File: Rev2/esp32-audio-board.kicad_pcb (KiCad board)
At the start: 4 copper layers, 37.5 x 70 mm, 129 parts, among them IC1 LP2985A-33DBVR, J2 JST S2B, J21 IO32_PAD0, J3 USB_C_Receptacle_USB2.0_16P, J5 IO32_PAD1, J6 IO33_PAD0, J7 IO33_PAD1, J8 IO25_PAD0, J9 IO25_PAD1, Q1 SS8050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

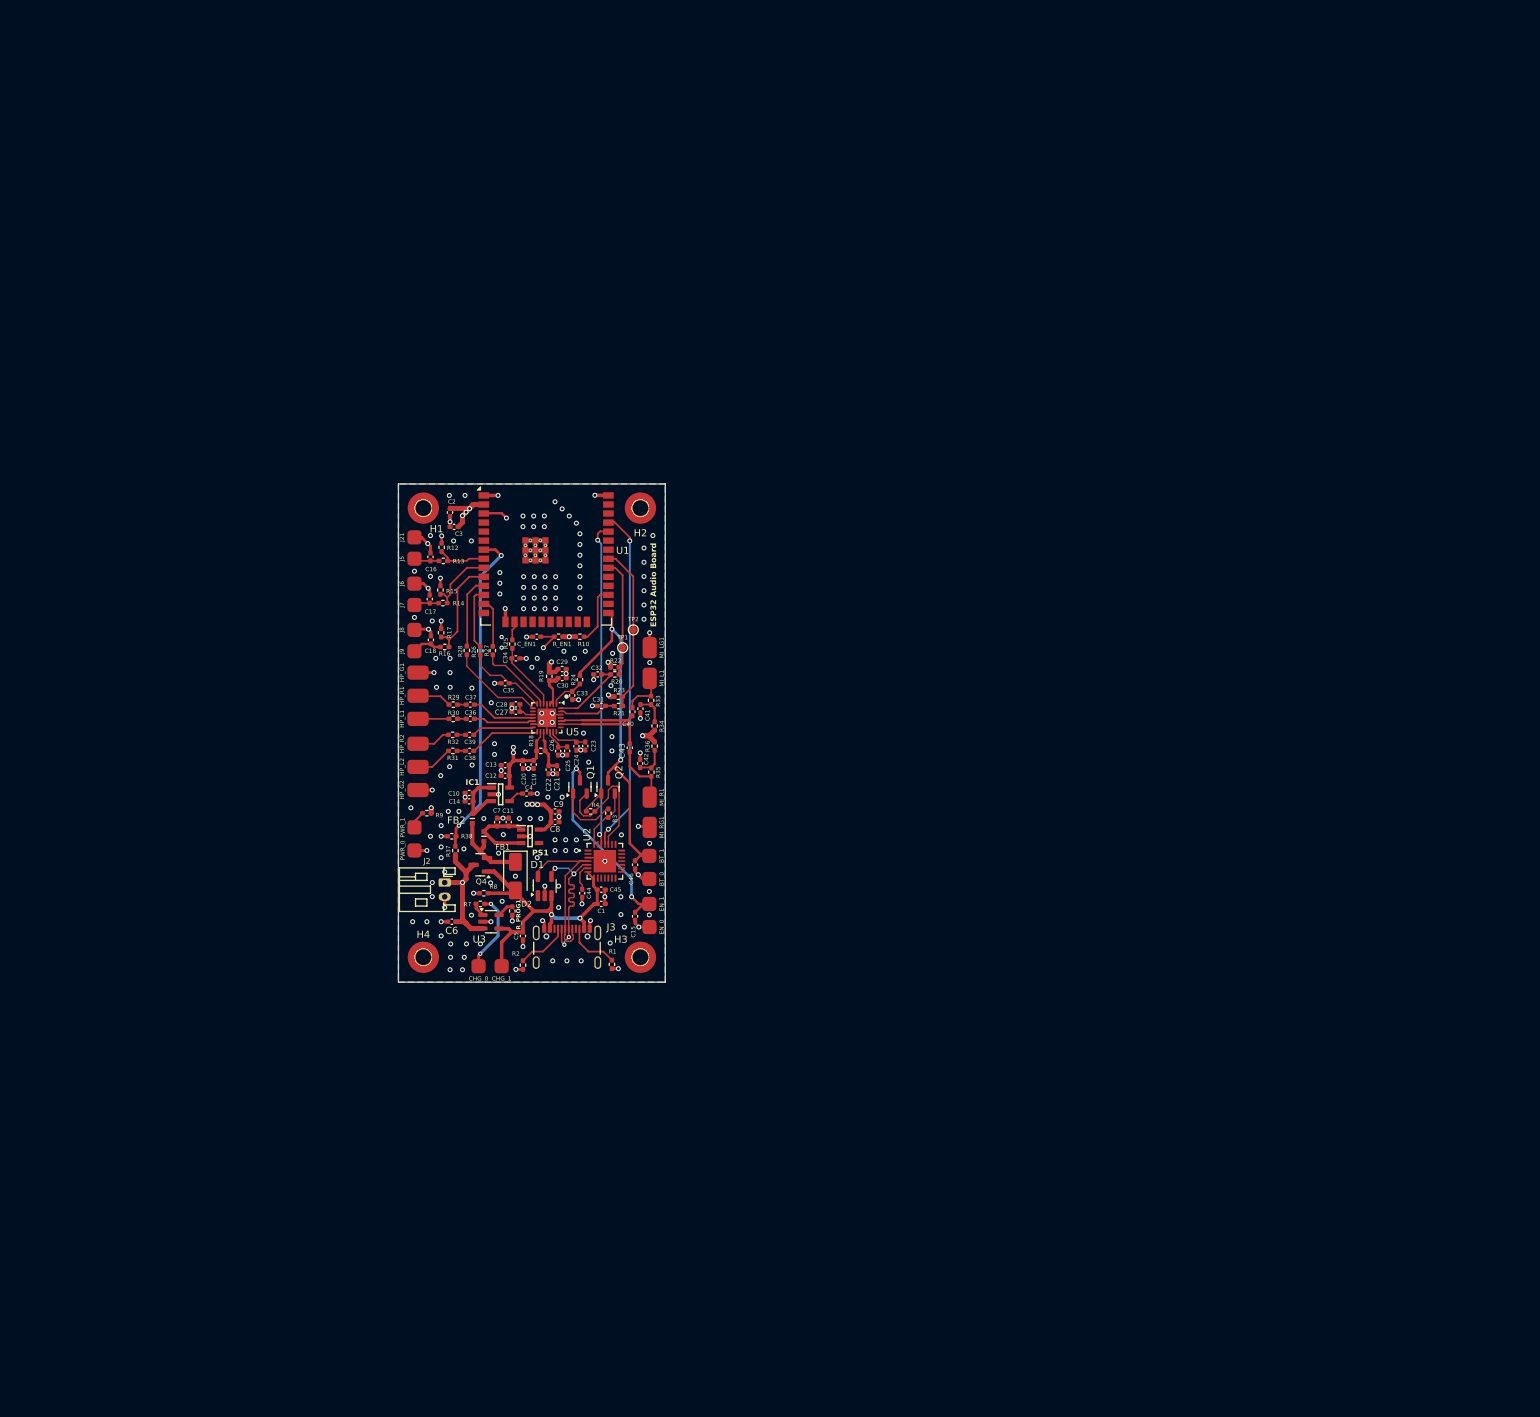
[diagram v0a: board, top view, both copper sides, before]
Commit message: esp32-audio-board: initial Rev2 PCB
Started working on the Rev2 PCB. Managed to get components
a lot closer and the PCB layout is more compact. The PCB
width got smaller by ~10mm.
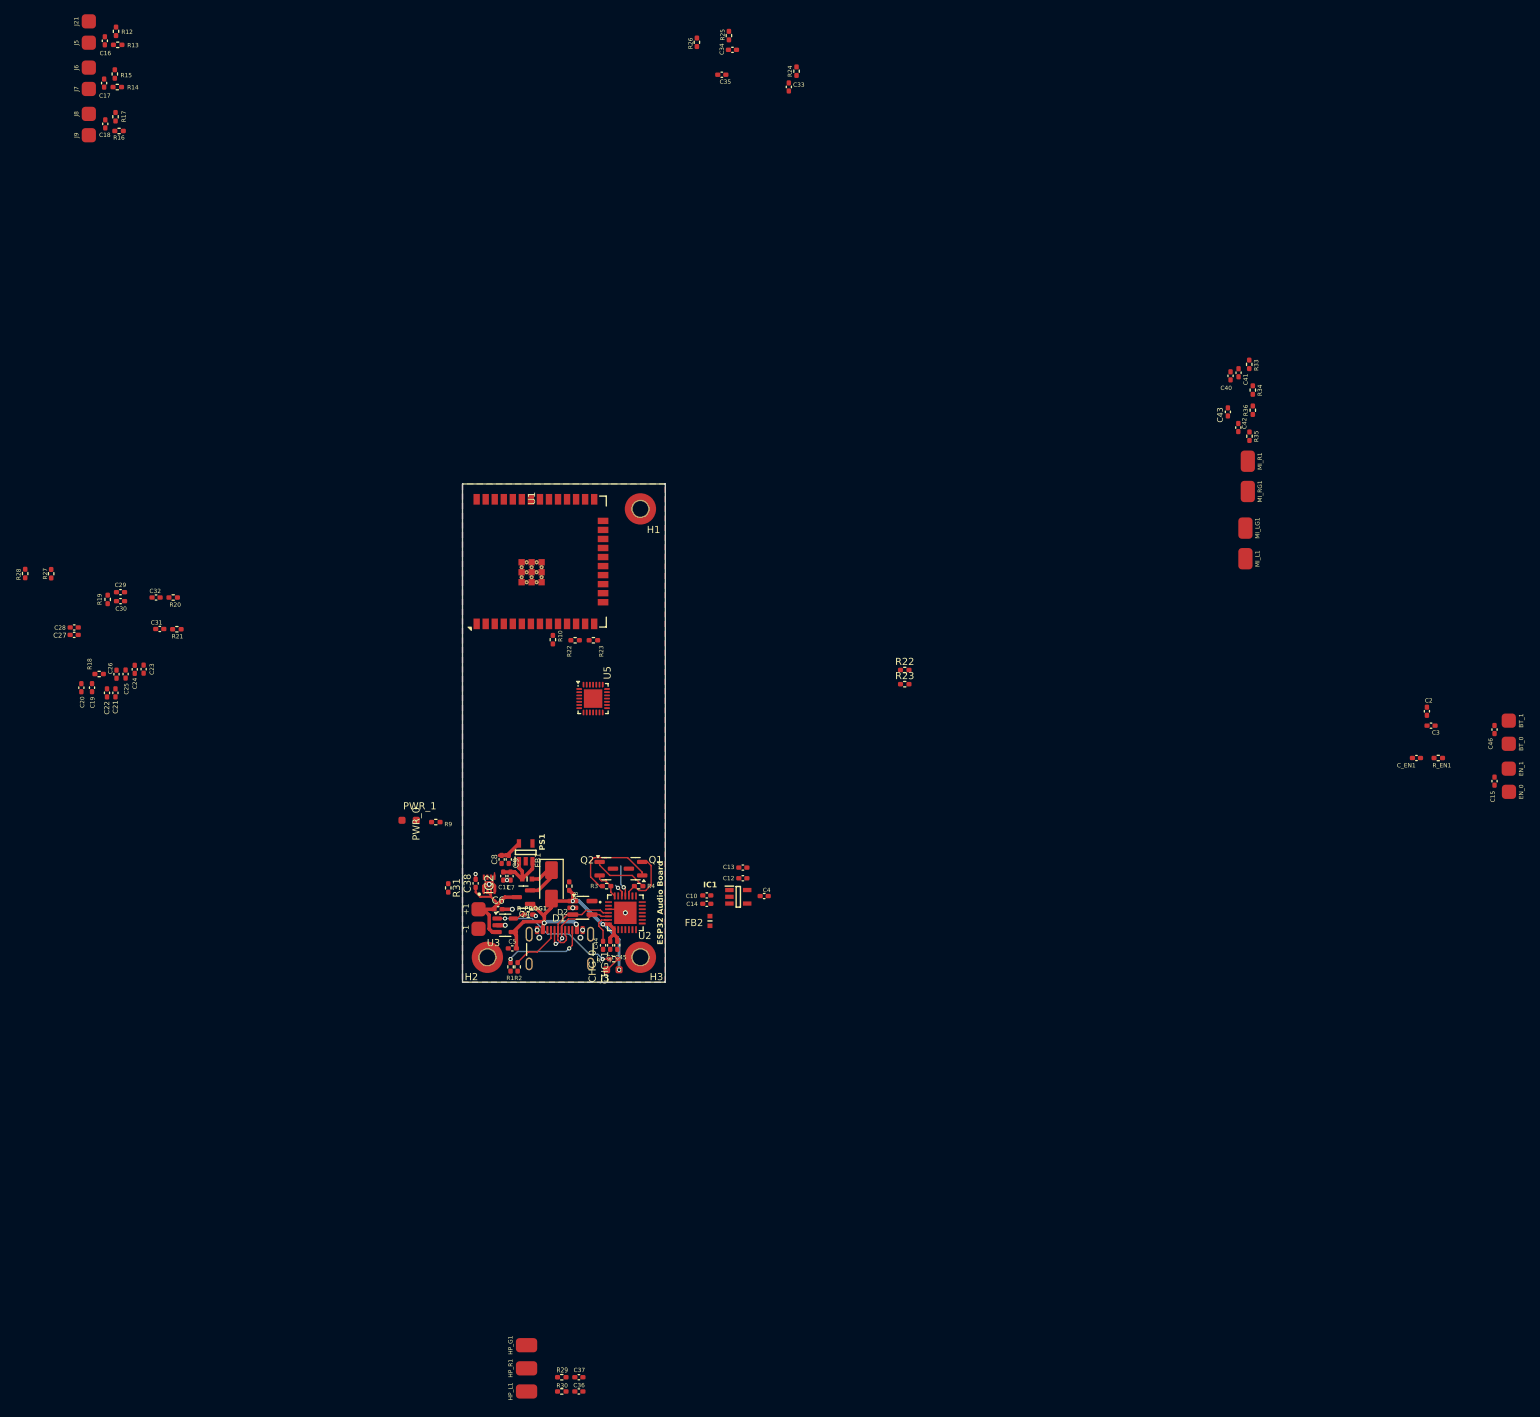
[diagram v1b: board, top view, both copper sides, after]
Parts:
- removed C39: 22uF/10%, Capacitor_SMD:C_0402_1005Metric_Pad0.74x0.62mm_HandSolder
- removed H4: MountingHole_Pad, MountingHole:MountingHole_2.2mm_M2_Pad_TopOnly
- removed HP_G2: HP_GND2, solderpads:SolderPad_SMD_2x3mm
- removed HP_L2: HP_LOUT2, solderpads:SolderPad_SMD_2x3mm
- removed HP_R2: HP_ROUT2, solderpads:SolderPad_SMD_2x3mm
- removed J2: JST S2B, Connector_JST:JST_PH_S2B-PH-K_1x02_P2.00mm_Horizontal
- removed R32: 33R/1%, Resistor_SMD:R_0402_1005Metric_Pad0.72x0.64mm_HandSolder
- removed R37, R38: 100K/1%, Resistor_SMD:R_0402_1005Metric_Pad0.72x0.64mm_HandSolder
- removed TP1: T_SCL, TestPoint:TestPoint_Pad_D1.0mm
- removed TP2: T_SDA, TestPoint:TestPoint_Pad_D1.0mm
- added +1: +, solderpads:SolderPad_SMD_2x2mm, F.Cu at (43.8, 105.2)
- added -1: -, solderpads:SolderPad_SMD_2x2mm, F.Cu at (43.8, 108.0)
- added IC2: MAX17048G+T10, max17048G:SON50P200X200X80-9N-D, F.Cu at (45.2, 101.8)
- added R22: 2K, Resistor_SMD:R_0402_1005Metric_Pad0.72x0.64mm_HandSolder, F.Cu at (103.6, 71.6)
- added R23: 2K, Resistor_SMD:R_0402_1005Metric_Pad0.72x0.64mm_HandSolder, F.Cu at (103.6, 73.6)
- C38: value 22uF/10% -> 0.1uF/10%
- CHG_0, CHG_1, PWR_0, PWR_1: footprint solderpads:SolderPad_SMD_2x2mm -> solderpads:SolderPad_SMD_1x1mm
- R31: value 33R/1% -> 2K
- moved C2 140.1 mm to (177.0, 77.4)
- moved C3 140.1 mm to (177.6, 79.5)
- moved C_EN1 124.8 mm to (175.5, 84.0)
- moved R_EN1 124.8 mm to (178.6, 84.0)
- moved BT_0 122.2 mm to (188.5, 82.0)
- moved BT_1 122.2 mm to (188.5, 78.8)
- moved C15 122.2 mm to (186.5, 87.2)
- moved C46 122.2 mm to (186.5, 80.0)
- moved EN_0 122.2 mm to (188.5, 88.8)
- moved EN_1 122.2 mm to (188.5, 85.5)
- moved R35 96.4 mm to (152.1, 38.8)
- moved C42 96.4 mm to (150.5, 37.6)
- moved MI_R1 96.4 mm to (151.8, 42.3)
- moved MI_RG1 96.4 mm to (151.8, 46.6)
- moved C40 96.4 mm to (149.4, 30.3)
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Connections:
- C38 pad 1: ES8388_LOUT2 -> VBAT
- C38 pad 2: Net-(C38-Pad2) -> GND
- D1 pad 1: unconnected-(D1-K-Pad1) -> VBUS
- D1 pad 3: VBUS -> /D+
- D1 pad 5: /D+ -> unconnected-(D1-K-Pad5)
- R22 pad 2: SCL -> SDA
- R23 pad 2: SDA -> SCL
- R24 pad 1: ESP-IO0 -> Serial-TX
- R31 pad 1: Net-(C38-Pad2) -> +3V3
- R31 pad 2: Net-(HP_L2-Pin_1) -> !ALRT
- U1 pad 7: ESP_IO35 -> !ALRT
- U5 pad 14: ES8388_ROUT2 -> unconnected-(U5-ROUT2-Pad14)
- U5 pad 15: ES8388_LOUT2 -> unconnected-(U5-LOUT2-Pad15)
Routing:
- net +3V3: track 119.9 -> 3.94 mm, vias 11 -> 0
- net ESP-EN: track 82.9 -> 0.00 mm, vias 4 -> 0
- net +3V3 Audio: track 76.1 -> 0.00 mm, vias 6 -> 0
- net GND: track 82.7 -> 10.8 mm, vias 187 -> 10
- net ESP-IO0: track 50.5 -> 0.00 mm, vias 2 -> 0
- net ESP_IO35: track 46.3 -> 0.00 mm, vias 2 -> 0
- net Serial-RX: track 48.4 -> 4.49 mm, vias 2 -> 1
- net Serial-TX: track 45.9 -> 2.58 mm, vias 2 -> 1
- net SDA: track 23.6 -> 0.00 mm
- net SCL: track 16.6 -> 0.00 mm
- net Net-(U3-STAT): track 1.95 -> 18.4 mm, vias 0 -> 2
- net ESP_IO25: track 14.4 -> 0.00 mm
- net Net-(U5-ASDOUT): track 13.4 -> 0.00 mm
- net ES8388_RIN1: track 12.3 -> 0.00 mm
- net ES8388_LRCK: track 11.7 -> 0.00 mm
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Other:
- board size 37.5 x 70 mm -> 28.5 x 70 mm

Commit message: esp32-audio-board: Rev2 PCB done
Completed the work on the Rev2 PCB.
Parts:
- removed HP_G1: HP_GND1, solderpads:SolderPad_SMD_2x3mm
- removed HP_L1: HP_LOUT1, solderpads:SolderPad_SMD_2x3mm
- removed HP_R1: HP_ROUT1, solderpads:SolderPad_SMD_2x3mm
- removed MI_L1: MIC_LIN1, solderpads:SolderPad_SMD_2x3mm
- removed MI_LG1: MIC_LIN1_GND, solderpads:SolderPad_SMD_2x3mm
- removed MI_R1: MIC_RIN1, solderpads:SolderPad_SMD_2x3mm
- removed MI_RG1: MIC_RIN1_GND, solderpads:SolderPad_SMD_2x3mm
- removed the R22 at (57.3, 67.5)
- removed the R23 at (59.9, 67.5)
- added HP_G2: HP_GND2, solderpads:SolderPad_SMD_1x2mm, F.Cu at (67.8, 93.2)
- added HP_L2: HP_LOUT2, solderpads:SolderPad_SMD_1x2mm, F.Cu at (67.8, 95.0)
- added HP_R2: HP_ROUT2, solderpads:SolderPad_SMD_1x2mm, F.Cu at (67.8, 96.8)
- added MI_L2: MIC_LIN2, solderpads:SolderPad_SMD_1x2mm, F.Cu at (68.0, 84.5)
- added MI_LG2: MIC_LIN2_GND, solderpads:SolderPad_SMD_1x2mm, F.Cu at (68.0, 82.8)
- added MI_R2: MIC_RIN2, solderpads:SolderPad_SMD_1x2mm, F.Cu at (68.0, 86.2)
- added MI_RG2: MIC_RIN2_GND, solderpads:SolderPad_SMD_1x2mm, F.Cu at (68.0, 88.0)
- BT_0, BT_1, EN_0, EN_1, J21, J5, J6, J7, J8, J9: footprint solderpads:SolderPad_SMD_2x2mm -> solderpads:SolderPad_SMD_1x1mm
- C36, C37: value 22uF/10% -> 47uF/10%
- R29, R30: value 33R/1% -> 10R/1%
- moved BT_1 145.8 mm to (42.8, 83.8)
- moved BT_0 144.8 mm to (43.8, 86.5)
- moved EN_0 144.8 mm to (43.8, 90.0)
- moved EN_1 144.8 mm to (43.8, 88.2)
- moved C46 142.1 mm to (44.5, 85.5)
- moved C15 142.0 mm to (44.5, 89.0)
- moved C3 133.3 mm to (44.2, 80.0)
- moved C2 132.8 mm to (44.3, 81.1), turned to 180 degrees
- moved R_EN1 131.6 mm to (47.1, 80.2)
- moved C_EN1 128.5 mm to (47.1, 81.3), turned to 0 degrees
- moved J21 119.2 mm to (68.6, 69.2), turned to -90 degrees
- moved J6 117.6 mm to (68.6, 73.6), turned to -90 degrees
- moved J8 116.7 mm to (68.6, 78.9), turned to -90 degrees
- moved J5 115.6 mm to (68.6, 67.3), turned to -90 degrees
- moved J7 114.1 mm to (68.6, 71.7), turned to -90 degrees
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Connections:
- C36 pad 1: ES8388_LOUT1 -> ES8388_LOUT2
- C37 pad 1: ES8388_ROUT1 -> ES8388_ROUT2
- C40 pad 1: ES8388_LIN1 -> ES8388_LIN2
- C43 pad 1: ES8388_RIN1 -> ES8388_RIN2
- R12 pad 1: ESP_IO32 -> ESP_IO34
- R13 pad 1: ESP_IO32 -> ESP_IO34
- R14 pad 1: ESP_IO33 -> ESP_IO35
- R15 pad 1: ESP_IO33 -> ESP_IO35
- R16 pad 1: ESP_IO25 -> ESP_IO23
- R17 pad 1: ESP_IO25 -> ESP_IO23
- U1 pad 10: ESP_IO25 -> DATA_IN
- U1 pad 11: DATA_IN -> WS
- U1 pad 12: WS -> DATA_OUT
- U1 pad 13: DATA_OUT -> BCK
- U1 pad 16: BCK -> unconnected-(U1-IO13-Pad16)
- U1 pad 30: SCL -> unconnected-(U1-IO18-Pad30)
- U1 pad 31: SDA -> unconnected-(U1-IO19-Pad31)
- U1 pad 37: unconnected-(U1-IO23-Pad37) -> ESP_IO23
- U1 pad 6: unconnected-(U1-IO34-Pad6) -> ESP_IO34
- U1 pad 7: !ALRT -> ESP_IO35
- U1 pad 8: ESP_IO32 -> SDA
- U1 pad 9: ESP_IO33 -> SCL
- U5 pad 11: ES8388_ROUT1 -> unconnected-(U5-ROUT1-Pad11)
- U5 pad 12: ES8388_LOUT1 -> unconnected-(U5-LOUT1-Pad12)
- U5 pad 14: unconnected-(U5-ROUT2-Pad14) -> ES8388_ROUT2
- U5 pad 15: unconnected-(U5-LOUT2-Pad15) -> ES8388_LOUT2
- U5 pad 21: unconnected-(U5-RIN2-Pad21) -> ES8388_RIN2
- U5 pad 22: unconnected-(U5-LIN2-Pad22) -> ES8388_LIN2
- U5 pad 23: ES8388_RIN1 -> unconnected-(U5-RIN1-Pad23)
- U5 pad 24: ES8388_LIN1 -> unconnected-(U5-LIN1-Pad24)
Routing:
- net +3V3: track 3.94 -> 100.7 mm, vias 0 -> 11
- net Serial-TX: track 2.58 -> 96.2 mm, vias 1 -> 2
- net Serial-RX: track 4.49 -> 67.8 mm, vias 1 -> 2
- net ESP-IO0: track 0.00 -> 61.9 mm, vias 0 -> 3
- net GND: track 10.8 -> 69.5 mm, vias 10 -> 48
- net +3V3 Audio: track 0.00 -> 50.7 mm, vias 0 -> 7
- net ESP_IO23: track 0.00 -> 42.1 mm, vias 0 -> 2
- net SDA: track 0.00 -> 39.8 mm, vias 0 -> 3
- net SCL: track 0.00 -> 39.7 mm, vias 0 -> 3
- net ESP-EN: track 0.00 -> 38.7 mm, vias 0 -> 2
- net ESP_IO34: track 0.00 -> 22.4 mm, vias 0 -> 4
- net ESP_IO35: track 0.00 -> 20.6 mm, vias 0 -> 4
- net ES8388_SCLK: track 0.00 -> 16.5 mm
- net ES8388_MCLK: track 0.00 -> 12.5 mm
- net DATA_IN: track 0.00 -> 11.7 mm
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- added copper zone on In2.Cu, net +3V3
- removed copper zone on In2.Cu, net VBAT
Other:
- board size 28.5 x 70 mm -> 28.5 x 62.4 mm
